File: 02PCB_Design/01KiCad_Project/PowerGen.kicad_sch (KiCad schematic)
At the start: 21 parts, among them J3 FCR7350R, J4 FCR7350R, U3 L6982, U4 AP2114D

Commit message: Changed Some Capacitor Sizes, Added Capacitors in Power Gen
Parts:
- added C10: 1uF, Capacitor_SMD:C_0603_1608Metric_Pad1.08x0.95mm_HandSolder, symbol Device:C
- added C11: 47uF, Capacitor_THT:CP_Radial_D8.0mm_P3.50mm, symbol Device:C
- added C19, C22: 4.7uF, Capacitor_SMD:C_0805_2012Metric_Pad1.18x1.45mm_HandSolder, symbol Device:C
- added C6: 1uF, Capacitor_SMD:C_0805_2012Metric_Pad1.18x1.45mm_HandSolder, symbol Device:C
- added C7: 100nF, Capacitor_SMD:C_0603_1608Metric_Pad1.08x0.95mm_HandSolder, symbol Device:C
- C20: renamed from C15; value 4.7uF -> 100nF; footprint Capacitor_SMD:C_0805_2012Metric_Pad1.18x1.45mm_HandSolder -> Capacitor_SMD:C_0603_1608Metric_Pad1.08x0.95mm_HandSolder
- C21: renamed from C16; value 4.7uF -> 100nF; footprint Capacitor_SMD:C_0805_2012Metric_Pad1.18x1.45mm_HandSolder -> Capacitor_SMD:C_0603_1608Metric_Pad1.08x0.95mm_HandSolder
- C5: footprint Capacitor_SMD:C_1210_3225Metric_Pad1.33x2.70mm_HandSolder -> Capacitor_THT:CP_Radial_D8.0mm_P3.50mm
- C9: renamed from C7; value 47uF -> 100nF; footprint Capacitor_THT:CP_Radial_D8.0mm_P3.50mm -> Capacitor_SMD:C_0603_1608Metric_Pad1.08x0.95mm_HandSolder
- renumbered C8 to C12, C9 to C13, C10 to C14, C11 to C15, C12 to C16, C13 to C17, C14 to C18, C17 to C23, C6 to C8
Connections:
- net +24V: now also C6.2, C7.2
- net +3.3V: now also C22.1
- net +5V: now also C10.1, C11.1, C19.1
- net GNDA: now also C10.2, C11.2, C19.2, C22.2, C6.1, C7.1
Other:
- moved on the sheet: C20, C21, C4, C5, C8, C9, L1, U3

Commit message: Reworked Half-Bridge and Power-Gen
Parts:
- C11, C5: footprint Capacitor_THT:CP_Radial_D8.0mm_P3.50mm -> Capacitor_SMD:C_1210_3225Metric_Pad1.33x2.70mm_HandSolder
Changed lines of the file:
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@@
       (effects (font (size 1.27 1.27)) (justify left))
     )
-    (property "Footprint" "Capacitor_THT:CP_Radial_D8.0mm_P3.50mm" (at 257.5052 58.42 0)
+    (property "Footprint" "Capacitor_SMD:C_1210_3225Metric_Pad1.33x2.70mm_HandSolder" (at 257.5052 58.42 0)
       (effects (font (size 1.27 1.27)) hide)
     )
@@
       (effects (font (size 1.27 1.27)) (justify left))
     )
-    (property "Footprint" "Capacitor_THT:CP_Radial_D8.0mm_P3.50mm" (at 140.0048 55.88 0)
-      (effects (font (size 1.27 1.27)) hide)
-    )
+    (property "Footprint" "Capacitor_SMD:C_1210_3225Metric_Pad1.33x2.70mm_HandSolder" (at 140.0048 55.88 0)
+      (effects (font (size 1.27 1.27)) hide)
+    )

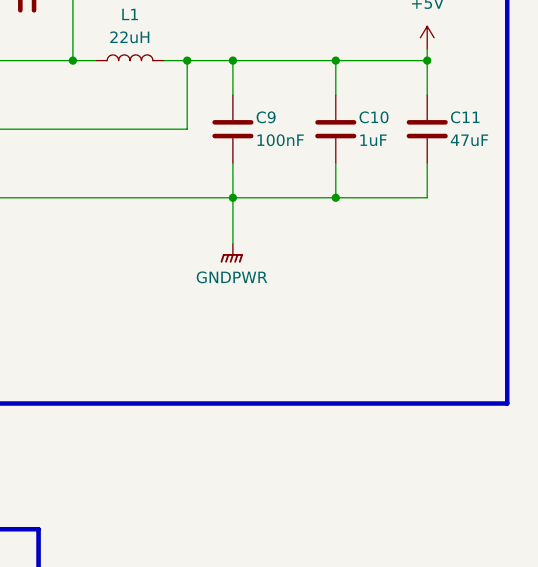
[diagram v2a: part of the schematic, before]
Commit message: sensor sheet & Power delivery
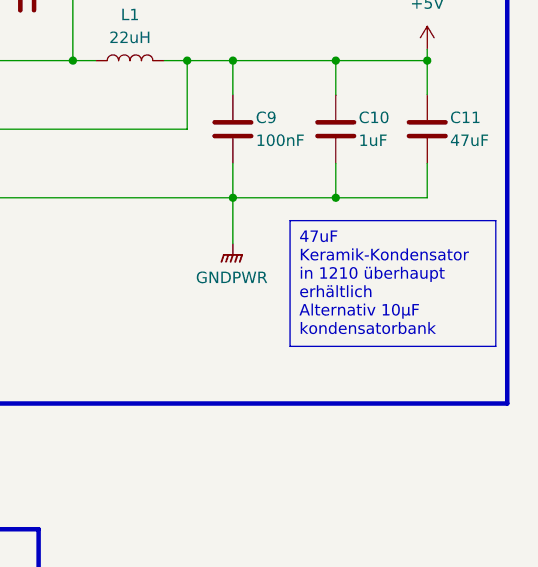
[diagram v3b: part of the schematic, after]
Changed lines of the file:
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@@
+    (effects (font (size 1.27 1.27)) (justify left top))
+  )
+  (text_box "47uF Keramik-Kondensator in 1210 überhaupt erhältlich \nAlternativ 10µF kondensatorbank\n"
+    (at 241.3 64.77 0) (size 22.86 13.97)
+    (stroke (width 0) (type default))
+    (fill (type none))
     (effects (font (size 1.27 1.27)) (justify left top))
   )

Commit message: edited footprints
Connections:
- net +24V: no longer J4.P$1, J4.P$3 (P$1), J4.P$4 (P$1), J4.P$5 (P$1)
- net GNDA: no longer J3.P$1, J3.P$3 (P$1), J3.P$4 (P$1), J3.P$5 (P$1)

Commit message: Edited some connectors
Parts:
- added D1, D2, D3: LED, LED_SMD:LED_0805_2012Metric_Pad1.15x1.40mm_HandSolder, symbol Device:LED
- added R43: 47k, Resistor_SMD:R_1206_3216Metric_Pad1.30x1.75mm_HandSolder, symbol Device:R
- added R44: 3.3k, Resistor_SMD:R_0805_2012Metric_Pad1.20x1.40mm_HandSolder, symbol Device:R
- added R45: 2.2k, Resistor_SMD:R_0805_2012Metric_Pad1.20x1.40mm_HandSolder, symbol Device:R
- J3, J4: value FCR7350R -> RS Pro 304-02-818; footprint Connector:Banana_Jack_1Pin -> MyFootprintLib:FCR7350
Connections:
- net +24V: now also R43.1
- net +3.3V: now also R45.1
- net +5V: now also R44.1
- net GNDA: now also D1.1 (K), D2.1 (K), D3.1 (K)
- new net: D1.2 (A), R43.2
- new net: D3.2 (A), R45.2
- new net: D2.2 (A), R44.2

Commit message: relayout in progress
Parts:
- removed D1, D2: LED, LED_SMD:LED_0805_2012Metric_Pad1.15x1.40mm_HandSolder, symbol Device:LED
- removed R43: 47k, Resistor_SMD:R_1206_3216Metric_Pad1.30x1.75mm_HandSolder, symbol Device:R
- removed R44: 3.3k, Resistor_SMD:R_0805_2012Metric_Pad1.20x1.40mm_HandSolder, symbol Device:R
- C10, C8: footprint Capacitor_SMD:C_0603_1608Metric_Pad1.08x0.95mm_HandSolder -> Capacitor_SMD:C_0805_2012Metric_Pad1.18x1.45mm_HandSolder
- U3: value L6982 -> L6982C50DR
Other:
- moved on the sheet: D3, R45
